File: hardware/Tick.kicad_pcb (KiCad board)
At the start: 2 copper layers, 33 x 22.5 mm, 41 parts, among them J1 Conn_01x03, J2 Conn_01x02, J3 Conn_01x04, J4 Conn_01x03, Q1 2N7002, Q2 2N7002, Q3 2N7002, Q4 2N7002, U1 LMR51430YDDCR, U2 THVD1400D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

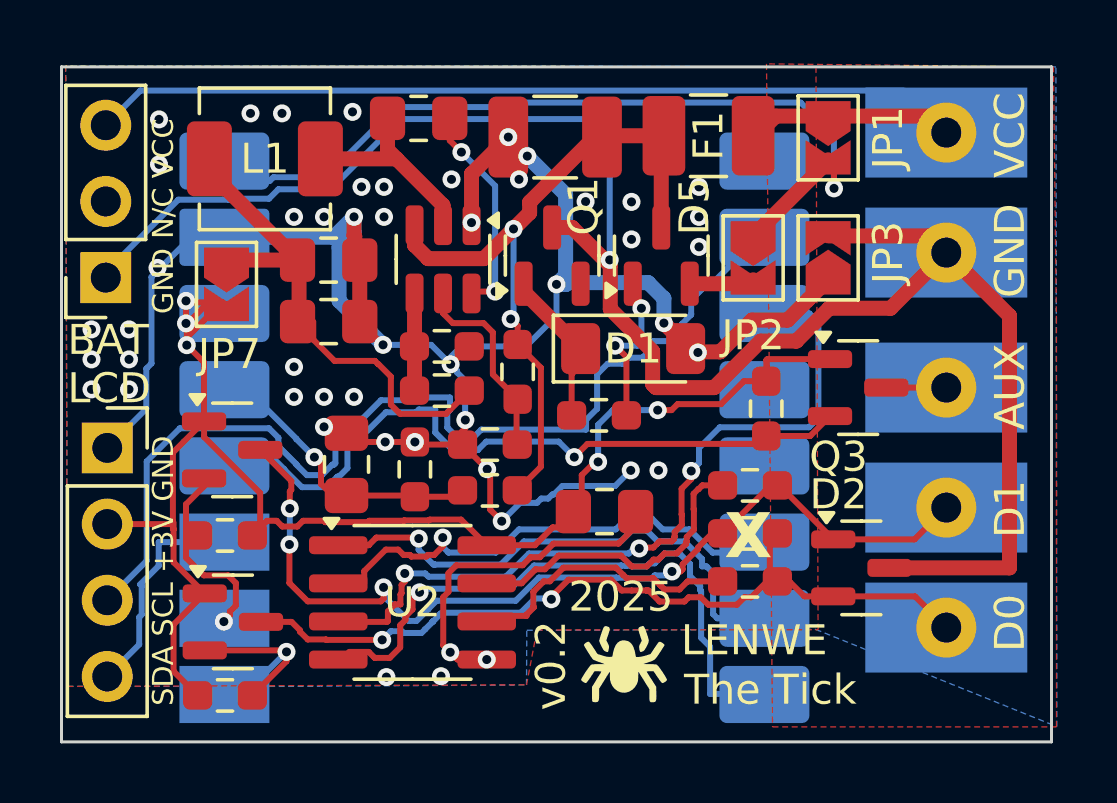
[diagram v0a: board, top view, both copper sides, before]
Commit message: added strong current sink on AUX
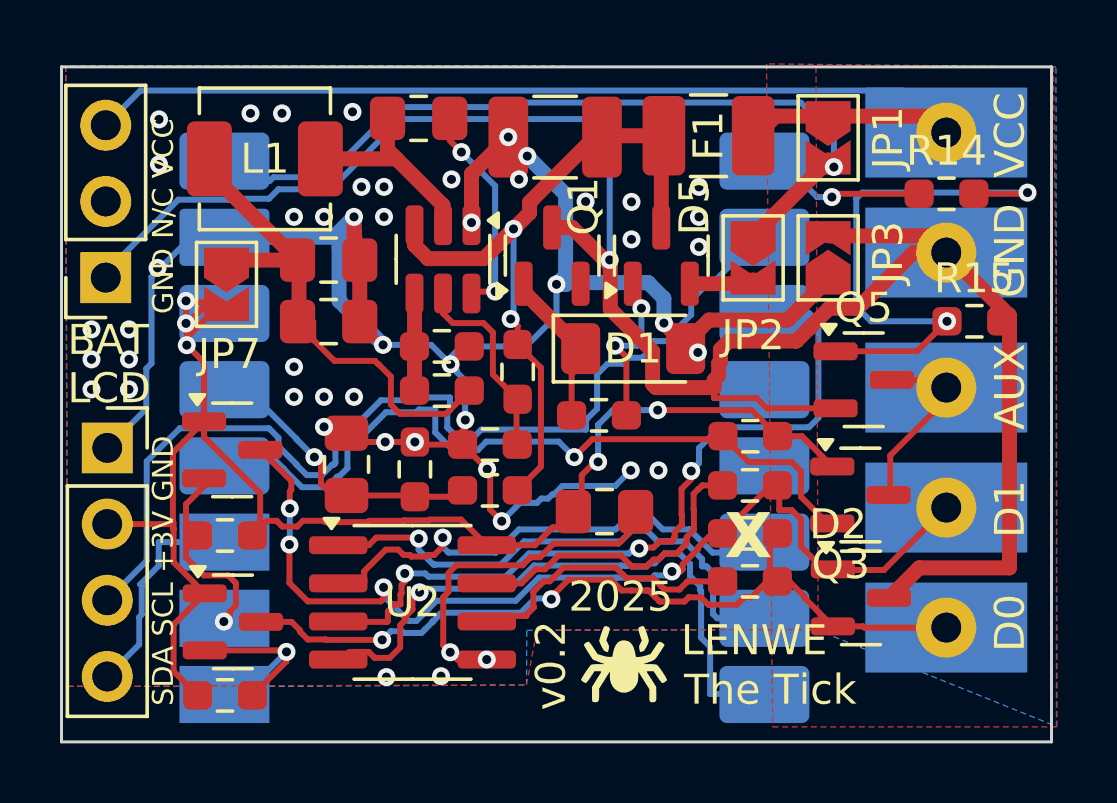
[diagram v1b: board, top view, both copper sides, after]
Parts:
- added Q5: 2N7002, Package_TO_SOT_SMD:SOT-23, F.Cu at (162.7, 101.9)
- added R14: 12k7, Resistor_SMD:R_0603_1608Metric_Pad0.98x0.95mm_HandSolder, F.Cu at (165.5, 95.7)
- added R15: 100k, Resistor_SMD:R_0603_1608Metric_Pad0.98x0.95mm_HandSolder, F.Cu at (166.4, 100.0)
- moved Q3 3.58 mm to (162.6, 105.8)
- moved R4 1.06 mm to (159.0, 103.8), turned to 180 degrees
- moved D2 1.00 mm to (162.7, 109.2)
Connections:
- U3 pad 5: unconnected-(U3-GPIO5-Pad5) -> AUX PULL
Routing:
- net Net-(Q5-G): track 0.00 -> 18.6 mm, vias 0 -> 2
- net GNDPWR: track 61.5 -> 67.3 mm
- net AUX PULL: track 0.00 -> 5.70 mm, vias 0 -> 1
- net AUX: track 2.00 -> 6.30 mm
- net AUX SENSE: track 23.3 -> 25.2 mm
- net D1: track 30.9 -> 32.7 mm
- net +5V: track 27.3 -> 25.9 mm
